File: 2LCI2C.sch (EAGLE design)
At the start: 38 parts, among them IC1 HX711-SOP16L, IC2 HX711-SOP16L, IC3 ATTINY84-SOIC14, J1 ICSP-PIN, J3 Load Cell, J4 Load Cell, Q1 2N3906, Q2 2N3906

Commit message: Changed sample rate from 10Hz to 80Hz
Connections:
- net GND: no longer IC1.RATE, IC2.RATE
- net VCC: now also IC1.RATE, IC2.RATE
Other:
- note added: "RATE pin pulled HIGH sets sample rate to 80Hz"
- note added: "XI pin pulled LOW enables internal oscillator"
- note removed: "Sample rate set to 10Hz by pulling RATE pin low"
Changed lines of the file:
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@@
 <plain>
 <frame x1="0" y1="0" x2="248.92" y2="185.42" columns="8" rows="5" layer="94"/>
-<text x="142.24" y="20.32" size="3.048" layer="94">2 x Load Cell I2C Interface</text>
+<text x="142.24" y="20.32" size="3.048" layer="94" font="vector">2 x Load Cell I2C Interface</text>
 <text x="172.72" y="14.478" size="1.778" layer="94">V1.0 (2020-06-30)</text>
 <text x="142.24" y="14.478" size="1.778" layer="94">SKU: 2LCI2C</text>
@@
 <wire x1="177.8" y1="119.38" x2="7.62" y2="119.38" width="0.254" layer="97" style="longdash"/>
 <wire x1="7.62" y1="119.38" x2="7.62" y2="177.8" width="0.254" layer="97" style="longdash"/>
-<text x="129.54" y="167.64" size="1.27" layer="97">Sample rate set to 10Hz by pulling RATE pin low</text>
+<text x="129.54" y="175.26" size="1.27" layer="97">RATE pin pulled HIGH sets sample rate to 80Hz</text>
 <text x="12.7" y="109.22" size="2.54" layer="94">Y Axis Load Cell Amplifier</text>
 <wire x1="7.62" y1="114.3" x2="177.8" y2="114.3" width="0.254" layer="97" style="longdash"/>
@@
 <wire x1="177.8" y1="55.88" x2="7.62" y2="55.88" width="0.254" layer="97" style="longdash"/>
 <wire x1="7.62" y1="55.88" x2="7.62" y2="114.3" width="0.254" layer="97" style="longdash"/>
-<text x="129.54" y="104.14" size="1.27" layer="97">Sample rate set to 10Hz by pulling RATE pin low</text>
+<text x="129.54" y="172.72" size="1.27" layer="97">XI pin pulled LOW enables internal oscillator</text>
 <text x="187.96" y="119.38" size="2.54" layer="94">I2C Header</text>
 <text x="12.7" y="48.26" size="2.54" layer="94">Processor</text>
@@
 <text x="10.16" y="86.36" size="1.778" layer="97">White</text>
 <text x="10.16" y="88.9" size="1.778" layer="97">Green</text>
+<text x="129.54" y="109.22" size="1.27" layer="97">XI pin pulled LOW enables internal oscillator</text>
+<text x="129.54" y="111.76" size="1.27" layer="97">RATE pin pulled HIGH sets sample rate to 80Hz</text>
 </plain>
 <instances>
@@
 <wire x1="149.86" y1="144.78" x2="149.86" y2="137.16" width="0.1524" layer="91"/>
 <junction x="149.86" y="137.16"/>
-<pinref part="IC2" gate="G$1" pin="RATE"/>
-<wire x1="147.32" y1="162.56" x2="149.86" y2="162.56" width="0.1524" layer="91"/>
-<wire x1="149.86" y1="162.56" x2="149.86" y2="144.78" width="0.1524" layer="91"/>
-<junction x="149.86" y="144.78"/>
 <pinref part="C12" gate="G$1" pin="2"/>
 <wire x1="165.1" y1="129.54" x2="165.1" y2="127" width="0.1524" layer="91"/>
@@
 <wire x1="149.86" y1="81.28" x2="149.86" y2="73.66" width="0.1524" layer="91"/>
 <junction x="149.86" y="73.66"/>
-<pinref part="IC1" gate="G$1" pin="RATE"/>
-<wire x1="147.32" y1="99.06" x2="149.86" y2="99.06" width="0.1524" layer="91"/>
-<wire x1="149.86" y1="99.06" x2="149.86" y2="81.28" width="0.1524" layer="91"/>
-<junction x="149.86" y="81.28"/>
 <pinref part="C6" gate="G$1" pin="2"/>
 <wire x1="165.1" y1="66.04" x2="165.1" y2="63.5" width="0.1524" layer="91"/>
@@
 <wire x1="114.3" y1="160.02" x2="114.3" y2="162.56" width="0.1524" layer="91"/>
 <junction x="114.3" y="162.56"/>
-<wire x1="114.3" y1="170.18" x2="165.1" y2="170.18" width="0.1524" layer="91"/>
+<wire x1="114.3" y1="170.18" x2="149.86" y2="170.18" width="0.1524" layer="91"/>
 <junction x="114.3" y="170.18"/>
 <pinref part="C12" gate="G$1" pin="1"/>
+<wire x1="149.86" y1="170.18" x2="165.1" y2="170.18" width="0.1524" layer="91"/>
 <wire x1="165.1" y1="170.18" x2="165.1" y2="137.16" width="0.1524" layer="91"/>
 <pinref part="Q2" gate="G$1" pin="E"/>
@@
 <wire x1="93.98" y1="170.18" x2="101.6" y2="170.18" width="0.1524" layer="91"/>
 <pinref part="P+9" gate="1" pin="VCC"/>
+<pinref part="IC2" gate="G$1" pin="RATE"/>
+<wire x1="147.32" y1="162.56" x2="149.86" y2="162.56" width="0.1524" layer="91"/>
+<wire x1="149.86" y1="162.56" x2="149.86" y2="170.18" width="0.1524" layer="91"/>
+<junction x="149.86" y="170.18"/>
 </segment>
 <segment>
@@
 <wire x1="114.3" y1="96.52" x2="114.3" y2="99.06" width="0.1524" layer="91"/>
 <junction x="114.3" y="99.06"/>
-<wire x1="114.3" y1="106.68" x2="165.1" y2="106.68" width="0.1524" layer="91"/>
+<wire x1="114.3" y1="106.68" x2="149.86" y2="106.68" width="0.1524" layer="91"/>
 <junction x="114.3" y="106.68"/>
 <pinref part="C6" gate="G$1" pin="1"/>
+<wire x1="149.86" y1="106.68" x2="165.1" y2="106.68" width="0.1524" layer="91"/>
 <wire x1="165.1" y1="106.68" x2="165.1" y2="73.66" width="0.1524" layer="91"/>
 <pinref part="Q1" gate="G$1" pin="E"/>
@@
 <wire x1="93.98" y1="106.68" x2="101.6" y2="106.68" width="0.1524" layer="91"/>
 <pinref part="P+7" gate="1" pin="VCC"/>
-</segment>
-<segment>
+<pinref part="IC1" gate="G$1" pin="RATE"/>
+<wire x1="147.32" y1="99.06" x2="149.86" y2="99.06" width="0.1524" layer="91"/>
+<wire x1="149.86" y1="99.06" x2="149.86" y2="106.68" width="0.1524" layer="91"/>
+<junction x="149.86" y="106.68"/>
+</segment>
+<segment>

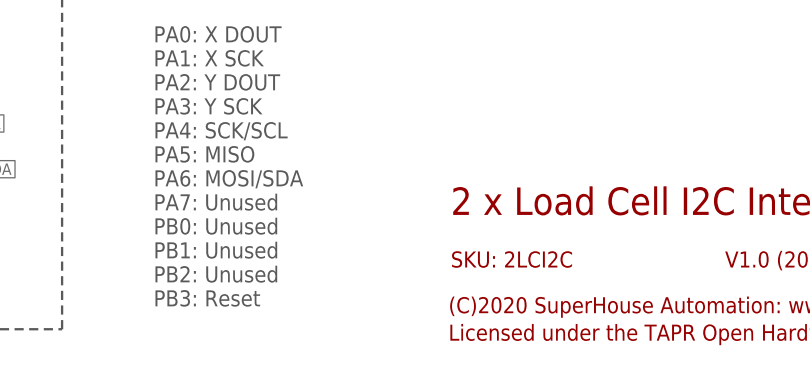
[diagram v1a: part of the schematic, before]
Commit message: Added fiducials for re-release v1.0
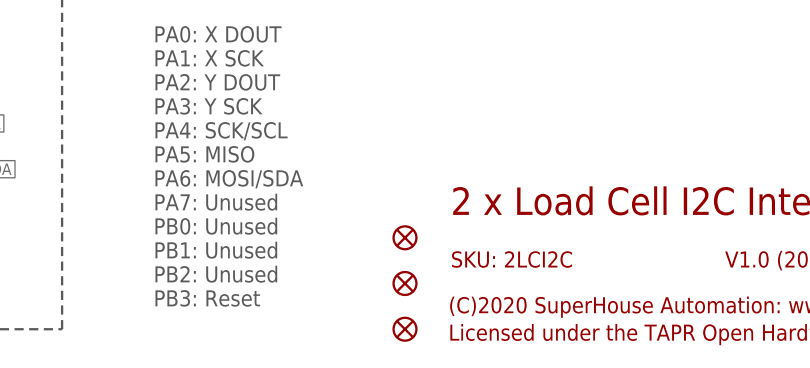
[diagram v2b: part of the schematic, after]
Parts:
- added U$10, U$11, U$5: FIDUCIAL1X2.5, SuperHouse-Symbols:FIDUCIAL1X2.5
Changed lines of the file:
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@@
 <part name="U$8" library="SuperHouse-SupplySymbols" library_urn="urn:adsk.eagle:library:11790503" deviceset="NC" device=""/>
 <part name="U$9" library="SuperHouse-SupplySymbols" library_urn="urn:adsk.eagle:library:11790503" deviceset="NC" device=""/>
+<part name="U$5" library="SuperHouse-Symbols" library_urn="urn:adsk.eagle:library:13228893" deviceset="FIDUCIAL" device="1X2.5" package3d_urn="urn:adsk.eagle:package:13228898/1"/>
+<part name="U$10" library="SuperHouse-Symbols" library_urn="urn:adsk.eagle:library:13228893" deviceset="FIDUCIAL" device="1X2.5" package3d_urn="urn:adsk.eagle:package:13228898/1"/>
+<part name="U$11" library="SuperHouse-Symbols" library_urn="urn:adsk.eagle:library:13228893" deviceset="FIDUCIAL" device="1X2.5" package3d_urn="urn:adsk.eagle:package:13228898/1"/>
 </parts>
 <sheets>
@@
 <instance part="U$8" gate="G$1" x="35.56" y="30.48" smashed="yes"/>
 <instance part="U$9" gate="G$1" x="35.56" y="25.4" smashed="yes"/>
+<instance part="U$5" gate="G$1" x="137.16" y="7.62" smashed="yes"/>
+<instance part="U$10" gate="G$1" x="137.16" y="12.7" smashed="yes"/>
+<instance part="U$11" gate="G$1" x="137.16" y="17.78" smashed="yes"/>
 </instances>
 <busses>
